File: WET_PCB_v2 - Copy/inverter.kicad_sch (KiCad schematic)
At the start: 36 parts, among them Q1 IRF530NPBF, Q2 IRF530NPBF, Q3 IRF530NPBF, Q4 IRF530NPBF, U3 IR2110, U4 IR2110

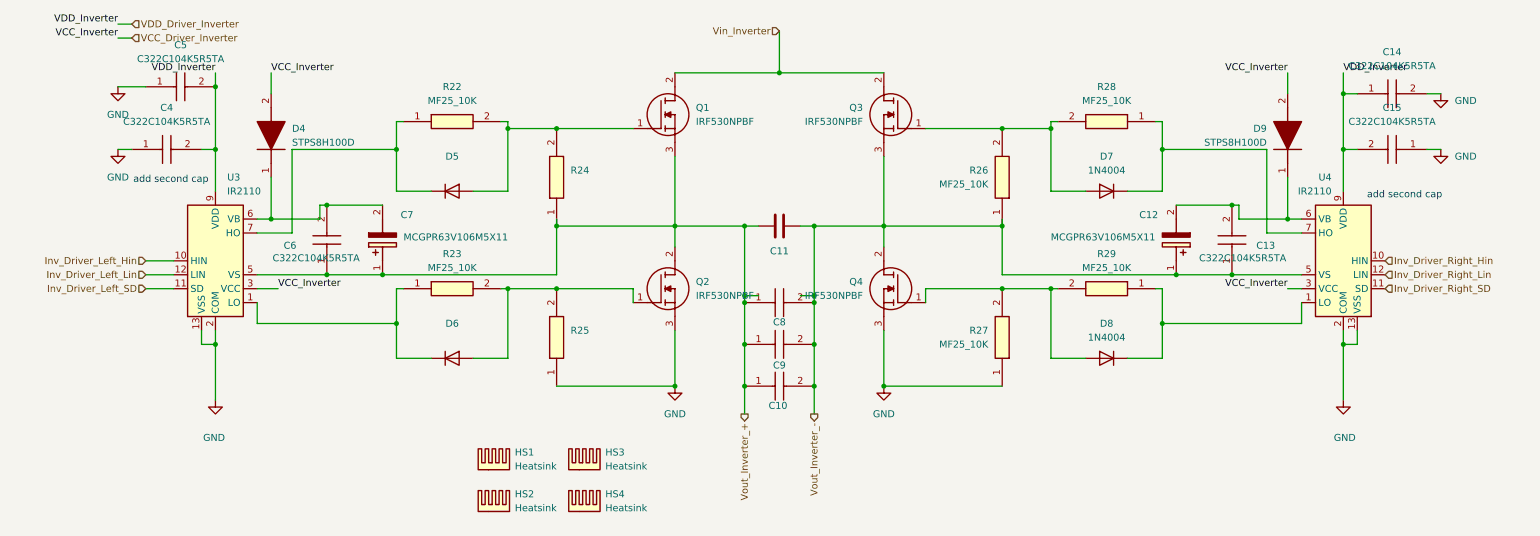
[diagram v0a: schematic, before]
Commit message: microcontroller to chip traces done
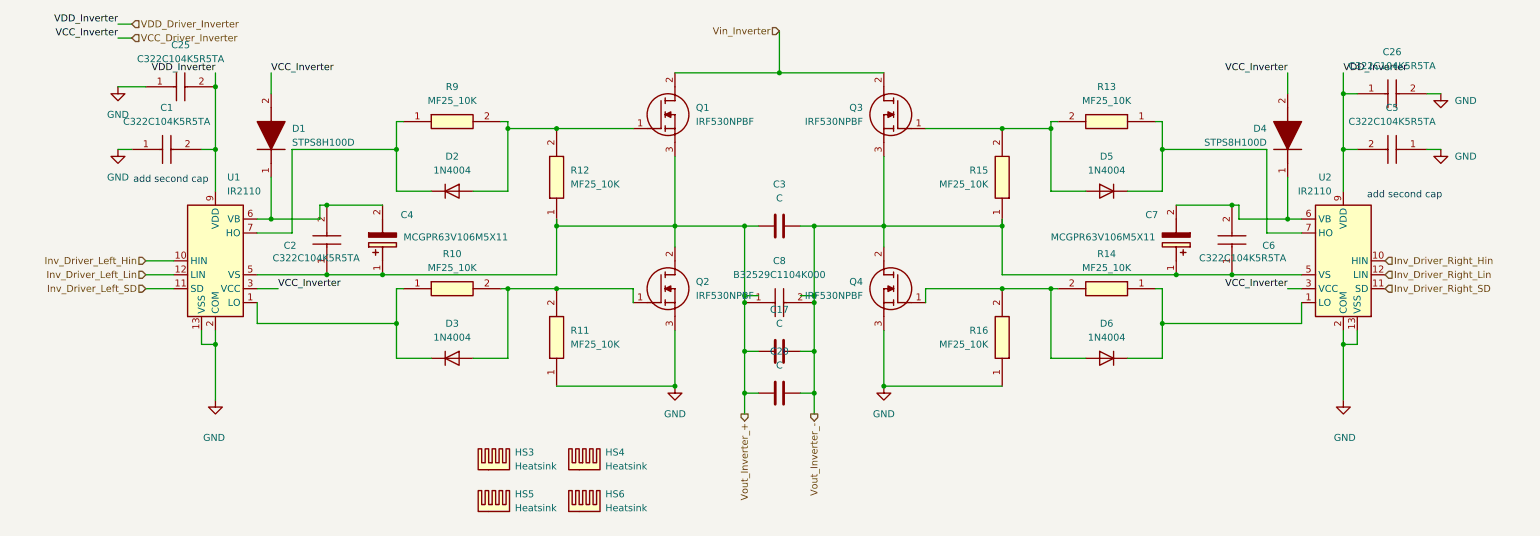
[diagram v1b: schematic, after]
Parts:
- removed C10: B32529C1104K000, Inductor_THT:L_Axial_L23.4mm_D12.7mm_P32.00mm_Horizontal_Vishay_IHA-203, symbol B32529C1104K000:B32529C1104K000
- removed C9: B32529C1104K000, Capacitor_THT:C_Rect_L24.0mm_W12.8mm_P22.50mm_MKT, symbol B32529C1104K000:B32529C1104K000
- added C17: C, Inductor_THT:L_Axial_L23.4mm_D12.7mm_P32.00mm_Horizontal_Vishay_IHA-203, symbol Device:C
- added C20: C, Capacitor_THT:C_Rect_L24.0mm_W12.8mm_P22.50mm_MKT, symbol Device:C
- renumbered C4 to C1, C6 to C2, C5 to C25, C14 to C26, C11 to C3, C7 to C4, C15 to C5, C13 to C6, C12 to C7, D4 to D1, D5 to D2, D6 to D3, D9 to D4, D7 to D5, D8 to D6, HS1 to HS3, HS3 to HS4, HS2 to HS5, HS4 to HS6, R23 to R10, R25 to R11, R24 to R12, R28 to R13, R29 to R14, R26 to R15, R27 to R16, R22 to R9, U3 to U1, U4 to U2
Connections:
- net Vout_Inverter_+: now also C17.1, C20.1
- net Vout_Inverter_-: now also C17.2, C20.2
